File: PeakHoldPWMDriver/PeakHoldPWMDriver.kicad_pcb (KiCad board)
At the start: 2 copper layers, 58 parts, among them Q1 BSP78, Q16 SMD-MOSFET-N-CH-55V-2.1A-AO34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, Q17 AO3401A, Q19 SMD-MOSFET-N-CH-55V-2.1A-AO34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, Q2 BSP78, Q20 AO3401A, Q21 SMD-MOSFET-N-CH-55V-2.1A-AO34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, Q22 SMD-MOSFET-N-CH-55V-2.1A-AO34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, Q23 AO3401A, Q24 AO3401A, Q3 BSP78, Q4 BSP78, U1 LM2901, U3 LM78M05_TO220, U5 TL431DBZ

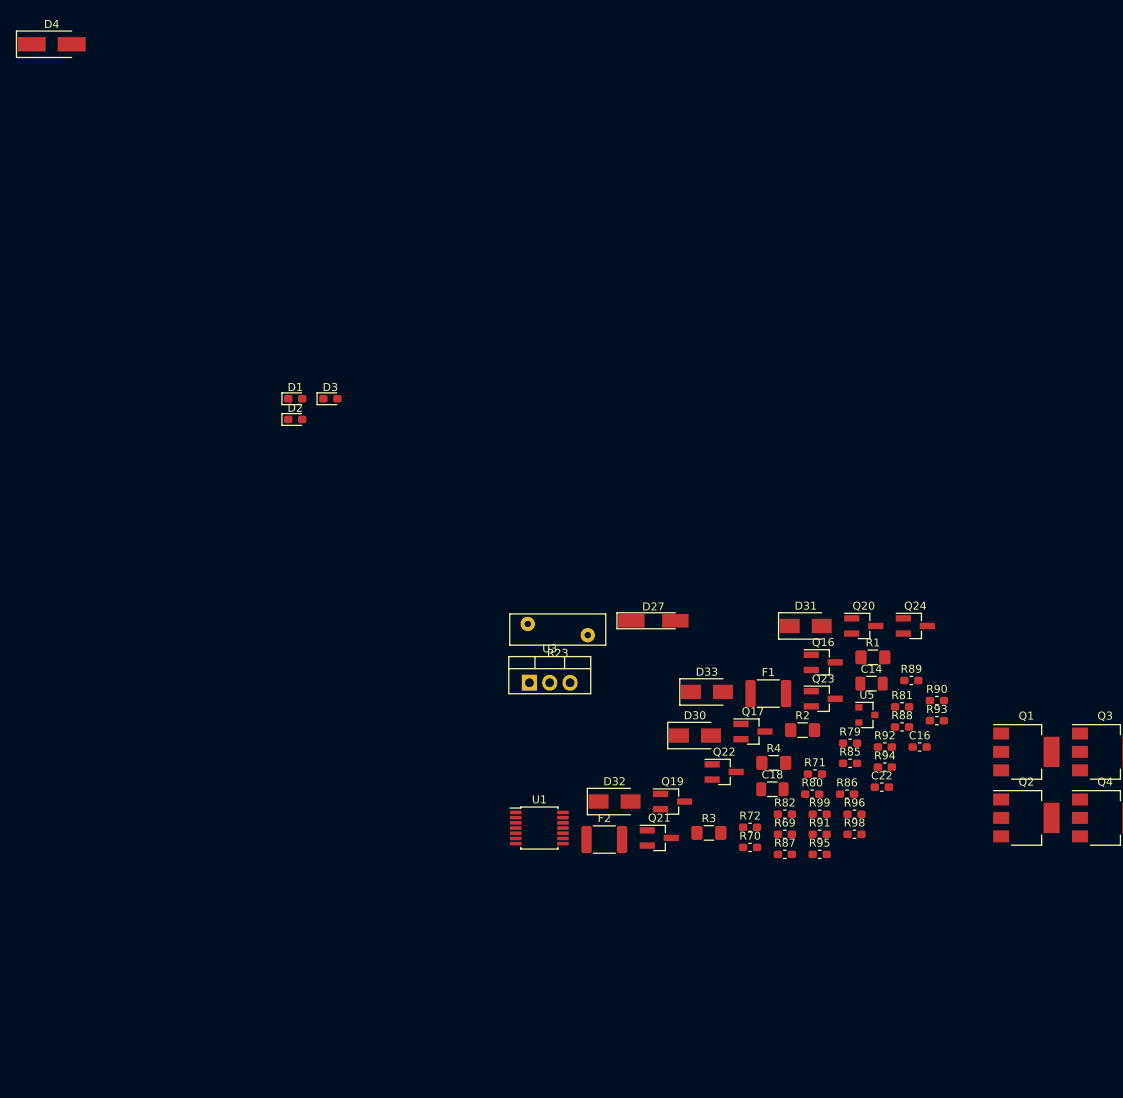
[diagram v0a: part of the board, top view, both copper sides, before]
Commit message: Stared implementing peak and hold driver. Also started in V0.6 of my board where the peak and hold driver is included
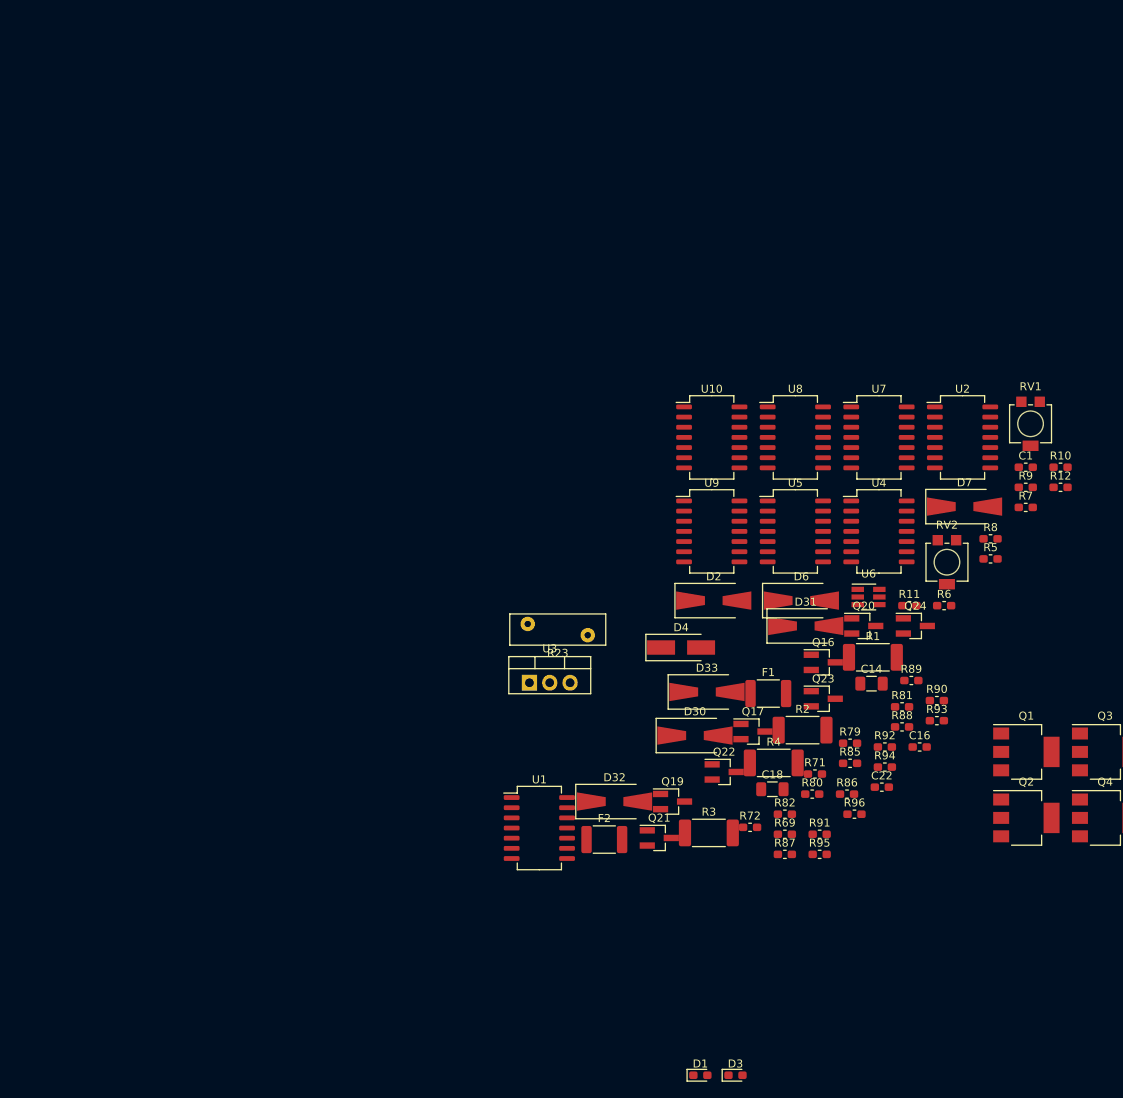
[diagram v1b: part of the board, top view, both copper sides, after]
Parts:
- removed D27: 3.6V, Diode_SMD:D_MiniMELF_Handsoldering
- removed R70: 82, Resistor_SMD:R_0603_1608Metric_Pad1.05x0.95mm_HandSolder
- removed R98: 2k49, Resistor_SMD:R_0603_1608Metric_Pad1.05x0.95mm_HandSolder
- removed R99: 1k8, Resistor_SMD:R_0603_1608Metric_Pad1.05x0.95mm_HandSolder
- added C1: 220nf, Capacitor_SMD:C_0603_1608Metric_Pad1.05x0.95mm_HandSolder, F.Cu at (80.7, -26.8)
- added D6: SS310, Diode_SMD:D_SMA-SMB_Universal_Handsoldering, F.Cu at (52.7, -10.2)
- added D7: SS310, Diode_SMD:D_SMA-SMB_Universal_Handsoldering, F.Cu at (73.1, -21.9)
- added R10: 1K, Resistor_SMD:R_0603_1608Metric_Pad1.05x0.95mm_HandSolder, F.Cu at (85.1, -26.8)
- added R11: 1K, Resistor_SMD:R_0603_1608Metric_Pad1.05x0.95mm_HandSolder, F.Cu at (66.2, -9.53)
- added R12: 1K, Resistor_SMD:R_0603_1608Metric_Pad1.05x0.95mm_HandSolder, F.Cu at (85.1, -24.3)
- added R5: 470, Resistor_SMD:R_0603_1608Metric_Pad1.05x0.95mm_HandSolder, F.Cu at (76.3, -15.4)
- added R6: 470, Resistor_SMD:R_0603_1608Metric_Pad1.05x0.95mm_HandSolder, F.Cu at (70.5, -9.53)
- added R7: 500k, Resistor_SMD:R_0603_1608Metric_Pad1.05x0.95mm_HandSolder, F.Cu at (80.7, -21.8)
- added R8: 500k, Resistor_SMD:R_0603_1608Metric_Pad1.05x0.95mm_HandSolder, F.Cu at (76.3, -17.9)
- added R9: 1K, Resistor_SMD:R_0603_1608Metric_Pad1.05x0.95mm_HandSolder, F.Cu at (80.7, -24.3)
- added RV1: R_POT_Small, Potentiometer_SMD:Potentiometer_Bourns_3314R-1_Vertical_Hole, F.Cu at (81.3, -32.3)
- added RV2: R_POT_Small, Potentiometer_SMD:Potentiometer_Bourns_3314R-1_Vertical_Hole, F.Cu at (70.9, -15.0)
- added U10: 74LS08, Package_SO:SO-14_5.3x10.2mm_P1.27mm, F.Cu at (41.5, -30.6)
- added U2: 74LS08, Package_SO:SO-14_5.3x10.2mm_P1.27mm, F.Cu at (72.8, -30.6)
- added U4: 74HC74, Package_SO:SO-14_5.3x10.2mm_P1.27mm, F.Cu at (62.4, -18.8)
- added U6: LTC6992, Package_TO_SOT_SMD:SOT-23-6_Handsoldering, F.Cu at (61.1, -10.6)
- added U7: 74LS08, Package_SO:SO-14_5.3x10.2mm_P1.27mm, F.Cu at (62.4, -30.6)
- added U8: 74LS08, Package_SO:SO-14_5.3x10.2mm_P1.27mm, F.Cu at (51.9, -30.6)
- added U9: 74LS08, Package_SO:SO-14_5.3x10.2mm_P1.27mm, F.Cu at (41.5, -18.8)
- D2: value BLUE -> SS310; footprint LED_SMD:LED_0603_1608Metric_Pad1.05x0.95mm_HandSolder -> Diode_SMD:D_SMA-SMB_Universal_Handsoldering
- D30, D31, D32, D33: footprint Diode_SMD:D_SMA -> Diode_SMD:D_SMA-SMB_Universal_Handsoldering
- Q17, Q20, Q23, Q24: value AO3401A -> TSM2309CX
- R1, R2, R3, R4: footprint Resistor_SMD:R_1206_3216Metric_Pad1.42x1.75mm_HandSolder -> Resistor_SMD:R_2512_6332Metric_Pad1.52x3.35mm_HandSolder
- U1: footprint Package_SO:TSSOP-14_4.4x5mm_P0.65mm -> Package_SO:SO-14_5.3x10.2mm_P1.27mm
- U5: value TL431DBZ -> 74LS08; footprint Package_TO_SOT_SMD:SOT-23 -> Package_SO:SO-14_5.3x10.2mm_P1.27mm
- moved D4 109.0 mm to (37.7, -4.30)
- moved D1 98.6 mm to (40.1, 49.2)
- moved D3 98.6 mm to (44.5, 49.2)
- moved D2 57.0 mm to (41.7, -10.2)
- moved U5 24.6 mm to (51.9, -18.8)
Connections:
- net PE11 renamed Net-(Q3-Pad1)
- net PE13 renamed Net-(Q4-Pad1)
- net PE14 renamed Net-(Q2-Pad1)
- net PE9 renamed Net-(Q1-Pad1)
- C14 pad 1: PWR_GND -> GND
- C16 pad 1: PWR_GND -> GND
- C18 pad 1: PWR_GND -> GND
- C22 pad 1: PWR_GND -> GND
- D1 pad 1: PWR_GND -> GND
- D2 pad 1: PWR_GND -> GND
- D3 pad 1: PWR_GND -> GND
- D5 pad 2: PWR_GND -> GND
- Q16 pad 2: PWR_GND -> GND
- Q19 pad 2: PWR_GND -> GND
- Q21 pad 2: PWR_GND -> GND
- Q22 pad 2: PWR_GND -> GND
- R1 pad 2: PWR_GND -> GND
- R2 pad 2: PWR_GND -> GND
- R23 pad 1: PWR_GND -> GND
- R3 pad 2: PWR_GND -> GND
- R4 pad 2: PWR_GND -> GND
- R72 pad 2: PWR_GND -> GND
- R79 pad 2: PWR_GND -> GND
- R80 pad 1: 3.3V -> 5V
- R85 pad 1: 3.3V -> 5V
- R88 pad 2: PWR_GND -> GND
- R89 pad 1: 3.3V -> 5V
- R90 pad 1: 3.3V -> 5V
- R95 pad 2: PWR_GND -> GND
- R96 pad 2: PWR_GND -> GND
- U1 pad 1: (no net) -> Net-(R10-Pad2)
- U1 pad 10: (no net) -> VREF
- U1 pad 11: (no net) -> Net-(Q3-Pad3)
- U1 pad 12: (no net) -> GND
- U1 pad 13: (no net) -> Net-(R11-Pad2)
- U1 pad 14: (no net) -> Net-(R12-Pad2)
- U1 pad 3: (no net) -> 5V
- U1 pad 4: Net-(U1-Pad4) -> VREF
- U1 pad 5: Net-(U1-Pad5) -> Net-(Q1-Pad3)
- U1 pad 6: (no net) -> VREF
- U1 pad 7: (no net) -> Net-(Q2-Pad3)
- U1 pad 8: (no net) -> VREF
- U1 pad 9: (no net) -> Net-(Q4-Pad3)
- U3 pad 2: PWR_GND -> GND
- U5 pad 1: 3.3V -> PWM
- U5 pad 2: Net-(R98-Pad1) -> PE12
- U5 pad 3: GND -> Net-(U5-Pad3)
